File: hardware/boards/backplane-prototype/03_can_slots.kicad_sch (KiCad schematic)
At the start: 15 parts, among them J1 SLOT_1, J2 XY308-2.54-3P / EXTERNAL CAN, J3 SLOT_2, J4 SLOT_3, J6 SLOT_4, J7 SLOT_5, J8 SLOT_6, U5 TCAN3413DR

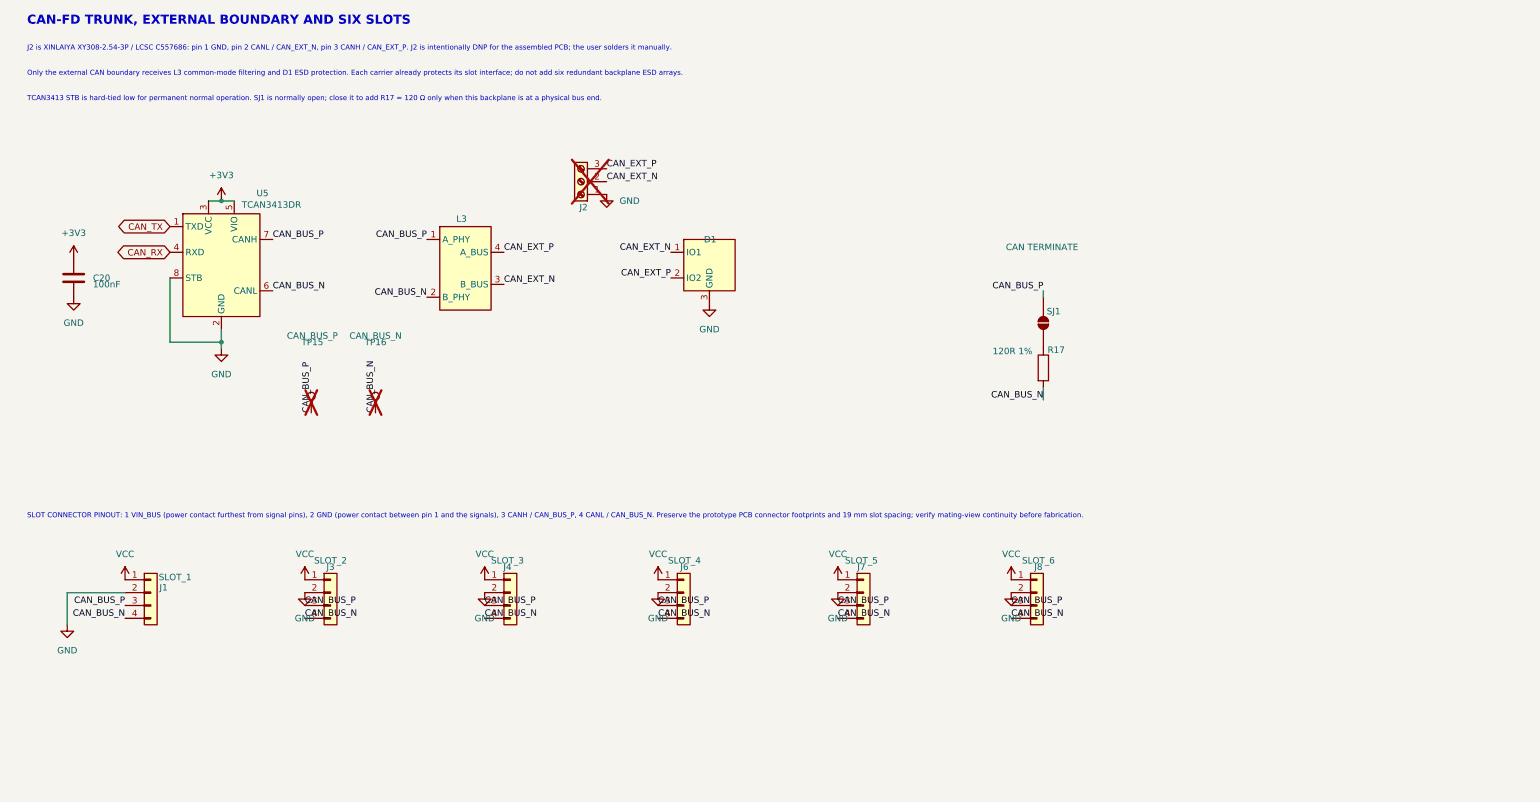
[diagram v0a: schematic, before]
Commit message: document CAN termination and align slot schematics
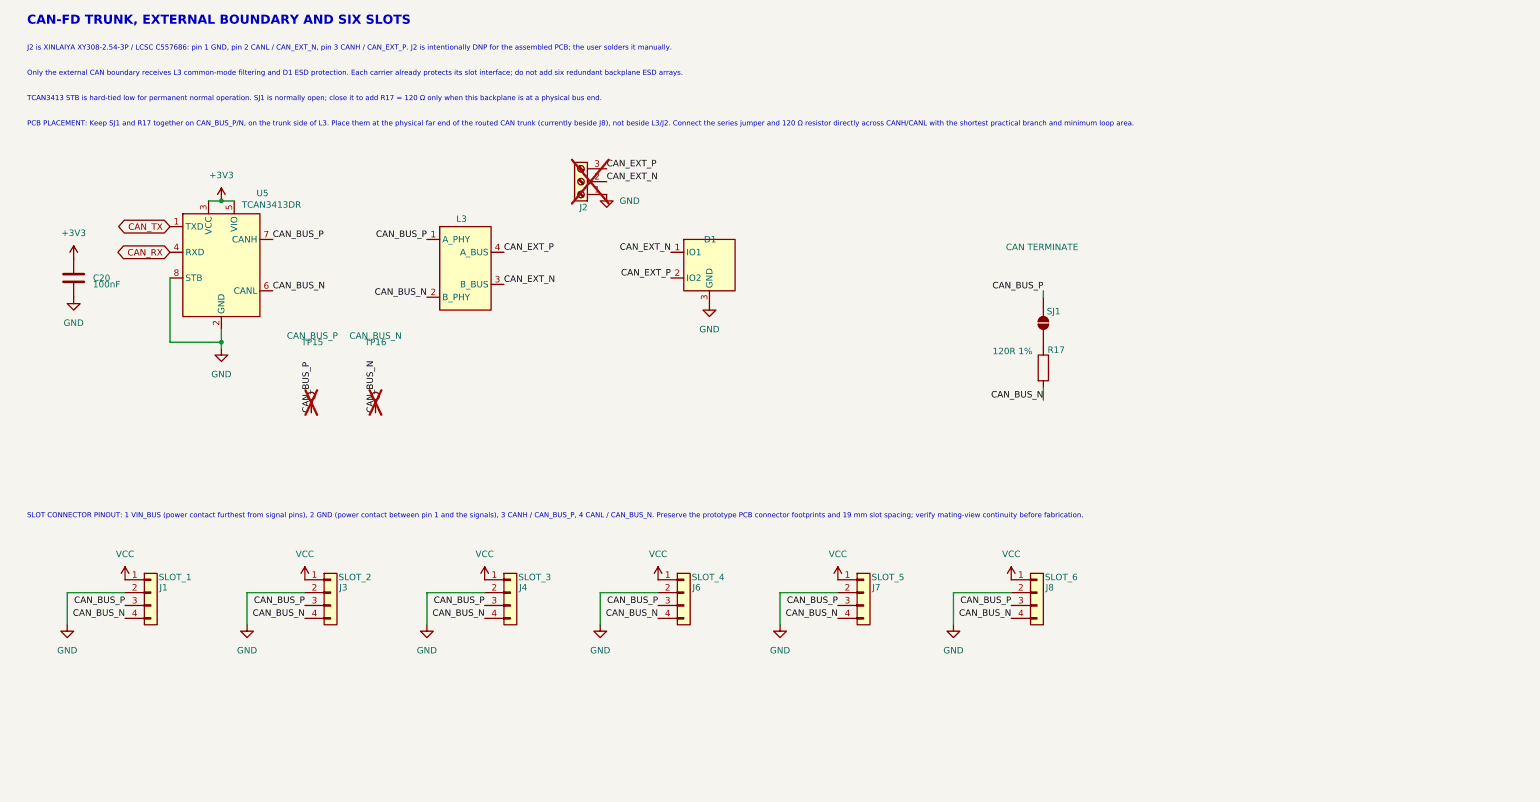
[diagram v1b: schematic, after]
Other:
- note added: "PCB PLACEMENT: Keep SJ1 and R17 together on CAN_BUS_P/N, on the trunk side of L3. Place them at the physical far end of the routed CAN trunk (currently beside J8), not beside L3/J2. Connect the series jumper and 120 Ω resistor directly across CANH/CANL with the shortest practical branch and minimum loop area."

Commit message: checkpoint: save schematic updates
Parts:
- SJ1: value CAN TERMINATE -> TERMINATION
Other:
- note added: "NOTES: - J2 is small screw terminal block. DNP for factory, user solders on. 1 GND 2 CANL / CAN_EXT_N 3 CANH / CAN_EXT_P - Only the external CAN boundary receives L3 common-mode filtering and D1 ESD protection. Each mate already protects its slot interface with ESD. - TCAN3413 STB is hard-tied low for permanent normal operation. LAYOUT: - Keep SJ1 and R17 together on CAN_BUS_P/N, on the trunk sid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"
- note added: "SLOT CONNECTOR is XT-30(+2) PINOUT: - 1 VIN_BUS (power contact furthest from signal pins) - 2 GND (power contact between pin 1 and the signals) - 3 CANH / CAN_BUS_P - 4 CANL / CAN_BUS_N"
- note removed: "J2 is XINLAIYA XY308-2.54-3P / LCSC C557686: pin 1 GND, pin 2 CANL / CAN_EXT_N, pin 3 CANH / CAN_EXT_P. J2 is intentionally DNP for the assembled PCB; the user solders it manually."
- note removed: "Only the external CAN boundary receives L3 common-mode filtering and D1 ESD protection. Each carrier already protects its slot interface; do not add six redundant backplane ESD arrays."
- note removed: "PCB PLACEMENT: Keep SJ1 and R17 together on CAN_BUS_P/N, on the trunk side of L3. Place them at the physical far end of the routed CAN trunk (currently beside J8), not beside L3/J2. Connect the series jumper and 120 Ω resistor directly across CANH/CANL with the shortest practical branch and minimum loop area."
- note removed: "SLOT CONNECTOR PINOUT: 1 VIN_BUS (power contact furthest from signal pins), 2 GND (power contact between pin 1 and the signals), 3 CANH / CAN_BUS_P, 4 CANL / CAN_BUS_N. Preserve the prototype PCB connector footprints and 19 mm slot spacing; verify mating-view continuity before fabrication."
- note removed: "TCAN3413 STB is hard-tied low for permanent normal operation. SJ1 is normally open; close it to add R17 = 120 Ω only when this backplane is at a physical bus end."
- moved on the sheet: C20, D1, J1, J2, J3, J4, J6, J7, J8, L3, R17, SJ1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

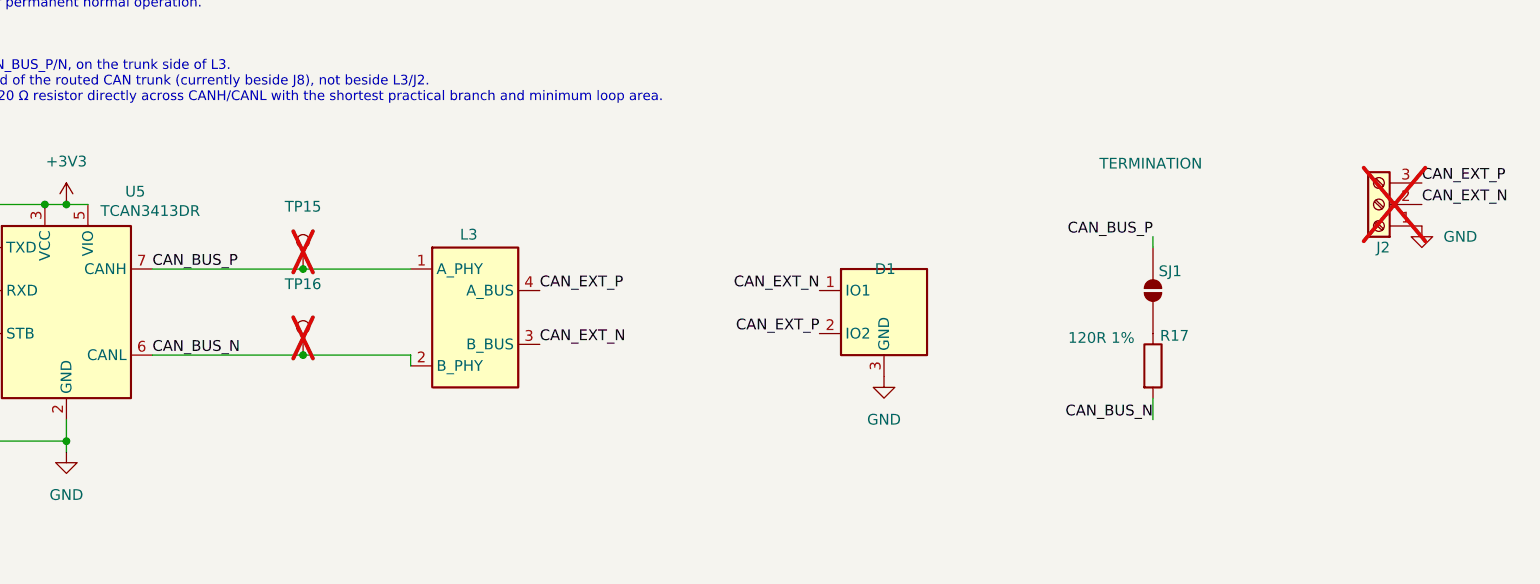
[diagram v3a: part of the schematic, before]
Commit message: checkpoint: save CAN schematic and layout updates
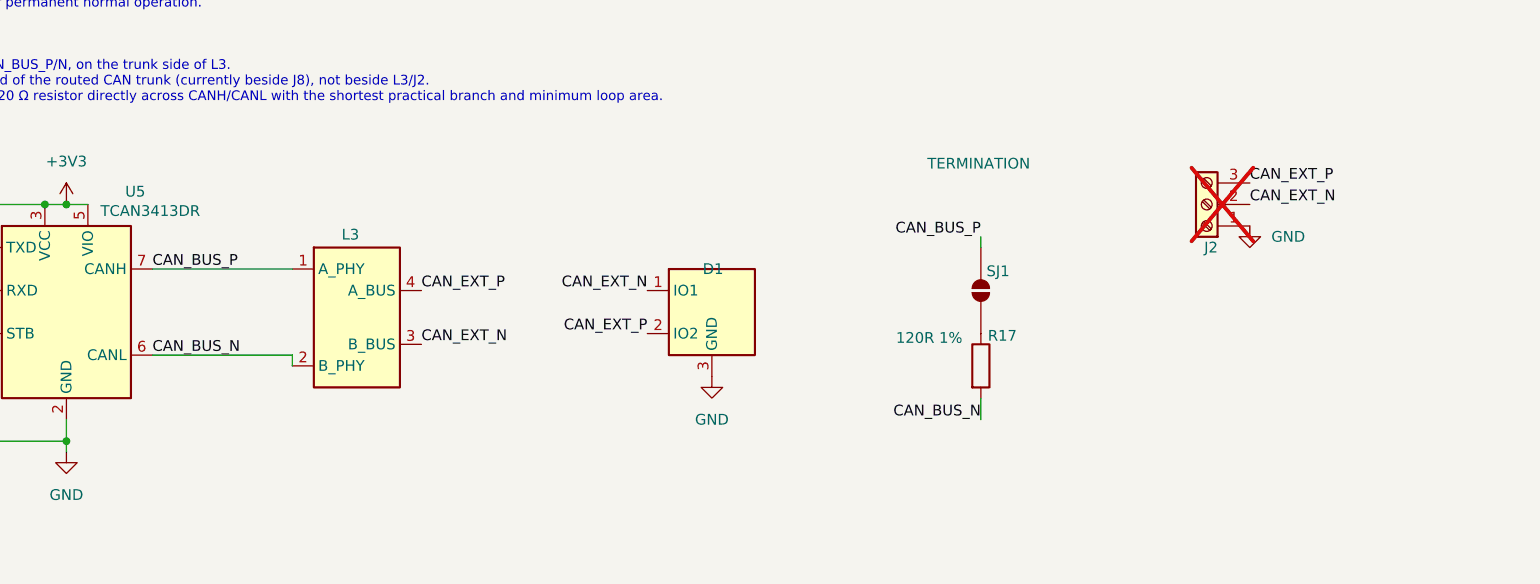
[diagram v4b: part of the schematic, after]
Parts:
- removed TP15: CAN_BUS_P, TestPoint:TestPoint_Pad_D1.5mm, symbol Connector:TestPoint
- removed TP16: CAN_BUS_N, TestPoint:TestPoint_Pad_D1.5mm, symbol Connector:TestPoint
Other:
- moved on the sheet: D1, J2, L3, R17, SJ1

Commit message: Fix routing clearances and production exports
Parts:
- SJ1: now left out of the parts list
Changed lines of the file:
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@@
 		(body_style 1)
 		(exclude_from_sim no)
-		(in_bom yes)
+		(in_bom no)
 		(on_board yes)
-		(in_pos_files yes)
+		(in_pos_files no)
 		(dnp no)
 		(property "Reference" "SJ1"

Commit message: Renumber backplane slot connectors J1 through J6
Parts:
- renumbered J3 to J2, J4 to J3, J6 to J4, J7 to J5, J8 to J6, J2 to J7
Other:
- note added: "NOTES: - J7 is small screw terminal block. DNP for factory, user solders on. 1 GND 2 CANL / CAN_EXT_N 3 CANH / CAN_EXT_P - Only the external CAN boundary receives L3 common-mode filtering and D1 ESD protection. Each mate already protects its slot interface with ESD. - TCAN3413 STB is hard-tied low for permanent normal operation. LAYOUT: - Keep SJ1 and R17 together on CAN_BUS_P/N, on the trunk sid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"
- note removed: "NOTES: - J2 is small screw terminal block. DNP for factory, user solders on. 1 GND 2 CANL / CAN_EXT_N 3 CANH / CAN_EXT_P - Only the external CAN boundary receives L3 common-mode filtering and D1 ESD protection. Each mate already protects its slot interface with ESD. - TCAN3413 STB is hard-tied low for permanent normal operation. LAYOUT: - Keep SJ1 and R17 together on CAN_BUS_P/N, on the trunk sid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"
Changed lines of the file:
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@@
 		)
 	)
-	(text "NOTES:\n\n  - J2 is small screw terminal block. DNP for factory, user solders on.\n    1 GND\n    2 CANL / CAN_EXT_N\n    3 CANH / CAN_EXT_P\n\n  - Only the external CAN boundary receives L3 common-mode filtering and D1 ESD protection.\n      Each mate already protects its slot interface with ESD.\n\n  - TCAN3413 STB is hard-tied low for permanent normal operation.\n\nLAYOUT:\n\n  - Keep SJ1 and R17 together on CAN_BUS_P/N, on the trunk side of L3.\n      Place them at the physical far end of the routed CAN trunk (currently beside J8), not beside L3/J2.\n      Connect the series jumper and 120 Ω resistor directly across CANH/CANL with the shortest practical branch and minimum loop area."
+	(text "NOTES:\n\n  - J7 is small screw terminal block. DNP for factory, user solders on.\n    1 GND\n    2 CANL / CAN_EXT_N\n    3 CANH / CAN_EXT_P\n\n  - Only the external CAN boundary receives L3 common-mode filtering and D1 ESD protection.\n      Each mate already protects its slot interface with ESD.\n\n  - TCAN3413 STB is hard-tied low for permanent normal operation.\n\nLAYOUT:\n\n  - Keep SJ1 and R17 together on CAN_BUS_P/N, on the trunk side of L3.\n      Place them at the physical far end of the routed CAN trunk (currently beside J6), not beside L3/J7.\n      Connect the series jumper and 120 Ω resistor directly across CANH/CANL with the shortest practical branch and minimum loop area."
 		(exclude_from_sim no)
 		(at 20.32 50.292 0)
@@
 		(in_pos_files yes)
 		(dnp no)
-		(property "Reference" "J8"
+		(property "Reference" "J6"
 			(at 154.94 155.194 0)
 			(show_name no)
@@
 			(project "backplane-prototype"
 				(path "/348cc909-6345-4013-9bef-98714057a65b/eb7e4e77-e42b-4b43-976a-f7a3e8147b95"
-					(reference "J8")
+					(reference "J6")
 					(unit 1)
 				)
@@
 		(in_pos_files yes)
 		(dnp no)
-		(property "Reference" "J6"
+		(property "Reference" "J4"
 			(at 107.95 155.194 0)
 			(show_name no)
@@
 			(project "backplane-prototype"
 				(path "/348cc909-6345-4013-9bef-98714057a65b/eb7e4e77-e42b-4b43-976a-f7a3e8147b95"
-					(reference "J6")
+					(reference "J4")
 					(unit 1)
 				)
@@
 		(in_pos_files yes)
 		(dnp no)
-		(property "Reference" "J4"
+		(property "Reference" "J3"
 			(at 83.82 155.194 0)
 			(show_name no)
@@
 			(project "backplane-prototype"
 				(path "/348cc909-6345-4013-9bef-98714057a65b/eb7e4e77-e42b-4b43-976a-f7a3e8147b95"
-					(reference "J4")
+					(reference "J3")
 					(unit 1)
 				)
@@
 		(in_pos_files yes)
 		(dnp no)
-		(property "Reference" "J3"
+		(property "Reference" "J2"
 			(at 60.96 155.194 0)
 			(show_name no)
@@
 			(project "backplane-prototype"
 				(path "/348cc909-6345-4013-9bef-98714057a65b/eb7e4e77-e42b-4b43-976a-f7a3e8147b95"
-					(reference "J3")
+					(reference "J2")
 					(unit 1)
 				)
@@
 		(in_pos_files yes)
 		(dnp no)
-		(property "Reference" "J7"
+		(property "Reference" "J5"
 			(at 132.08 155.194 0)
 			(show_name no)
@@
 			(project "backplane-prototype"
 				(path "/348cc909-6345-4013-9bef-98714057a65b/eb7e4e77-e42b-4b43-976a-f7a3e8147b95"
-					(reference "J7")
+					(reference "J5")
 					(unit 1)
 				)
@@
 		(in_pos_files yes)
 		(dnp yes)
-		(property "Reference" "J2"
+		(property "Reference" "J7"
 			(at 192.27 67.31 0)
 			(show_name no)
@@
 			(project "backplane-prototype"
 				(path "/348cc909-6345-4013-9bef-98714057a65b/eb7e4e77-e42b-4b43-976a-f7a3e8147b95"
-					(reference "J2")
+					(reference "J7")
 					(unit 1)
 				)

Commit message: Resolve backplane production-preflight issues
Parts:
- J1: value SLOT_1 -> XT30U_2+2; now not fitted
- J2: value SLOT_2 -> XT30U_2+2; now not fitted
- J3: value SLOT_3 -> XT30U_2+2; now not fitted
- J4: value SLOT_4 -> XT30U_2+2; now not fitted
- J5: value SLOT_5 -> XT30U_2+2; now not fitted
- J6: value SLOT_6 -> XT30U_2+2; now not fitted
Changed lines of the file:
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@@
 		(on_board yes)
 		(in_pos_files yes)
-		(dnp no)
+		(dnp yes)
 		(property "Reference" "J1"
 			(at 38.1 155.194 0)
@@
 			)
 		)
-		(property "Value" "SLOT_1"
+		(property "Value" "XT30U_2+2"
 			(at 40.386 153.162 0)
 			(show_name no)
@@
 		(on_board yes)
 		(in_pos_files yes)
-		(dnp no)
+		(dnp yes)
 		(property "Reference" "J6"
 			(at 154.94 155.194 0)
@@
 			)
 		)
-		(property "Value" "SLOT_6"
+		(property "Value" "XT30U_2+2"
 			(at 157.226 153.162 0)
 			(show_name no)
@@
 		(on_board yes)
 		(in_pos_files yes)
-		(dnp no)
+		(dnp yes)
 		(property "Reference" "J4"
 			(at 107.95 155.194 0)
@@
 			)
 		)
-		(property "Value" "SLOT_4"
+		(property "Value" "XT30U_2+2"
 			(at 110.236 153.162 0)
 			(show_name no)
@@
 		(on_board yes)
 		(in_pos_files yes)
-		(dnp no)
+		(dnp yes)
 		(property "Reference" "J3"
 			(at 83.82 155.194 0)
@@
 			)
 		)
-		(property "Value" "SLOT_3"
+		(property "Value" "XT30U_2+2"
 			(at 86.106 153.162 0)
 			(show_name no)
@@
 		(on_board yes)
 		(in_pos_files yes)
-		(dnp no)
+		(dnp yes)
 		(property "Reference" "J2"
 			(at 60.96 155.194 0)
@@
 			)
 		)
-		(property "Value" "SLOT_2"
+		(property "Value" "XT30U_2+2"
 			(at 63.246 153.162 0)
 			(show_name no)
@@
 		(on_board yes)
 		(in_pos_files yes)
-		(dnp no)
+		(dnp yes)
 		(property "Reference" "J5"
 			(at 132.08 155.194 0)
@@
 			)
 		)
-		(property "Value" "SLOT_5"
+		(property "Value" "XT30U_2+2"
 			(at 134.366 153.162 0)
 			(show_name no)
